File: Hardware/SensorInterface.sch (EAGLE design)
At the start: 57 parts, among them J3 CONN_32.54_SCREW, J4 CONN_32.54_SCREW, J5 CONN_42.54_SCREW, Q1 DMG3404, Q2 2N7002, Q3 2N7002, Q4 DMG3404, Q5 DMG3404, U10 SN74AHC1G86DCK, U11 MCP6041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

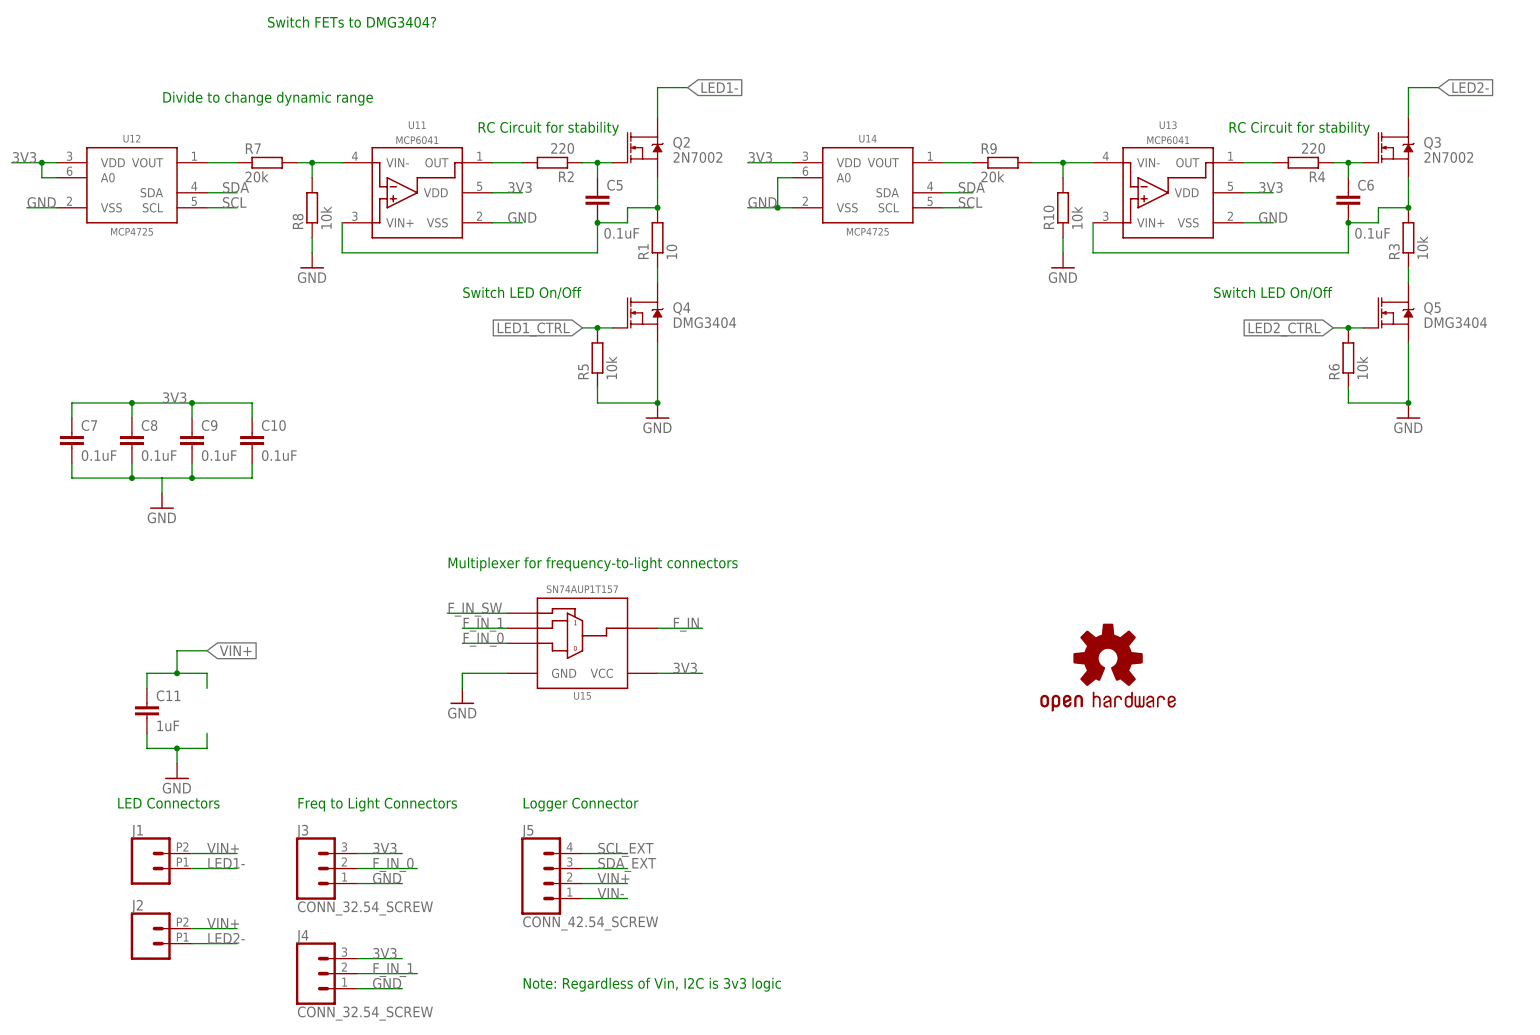
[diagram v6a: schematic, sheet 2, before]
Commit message: Updated breakouts and main board, schematic v0.1 updates
Updated schematic for main unit to v0.1, incorporating updates from testing of v0.0 unit
Minor updates to breakout boards, adding passives and updating components
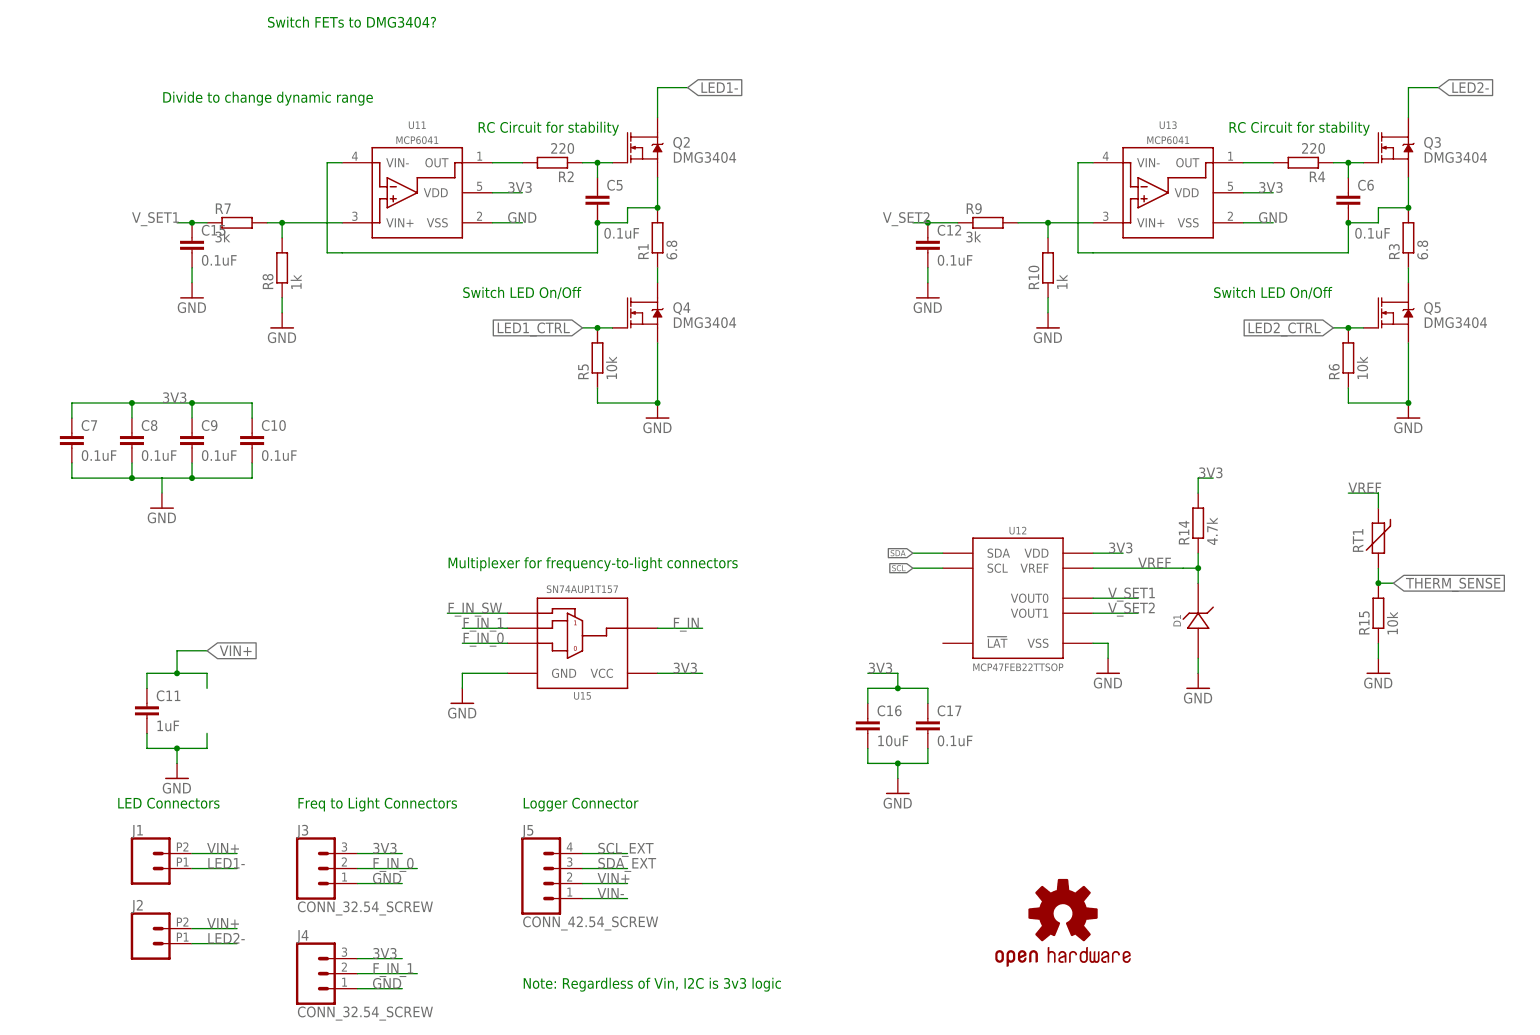
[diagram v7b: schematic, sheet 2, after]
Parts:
- removed U$3: ATTINY441/841841SOIC, bschulz:ATTINY441/841841SOIC
- added C12, C15: 0.1uF, bschulz_passives:C-EU0.1UFC0603
- added C16: 10uF, bschulz_passives:C-EUC0805
- added C17: 0.1uF, bschulz_passives:C-EUC0603
- added D1: (no value), bschulz:LM40402.048
- added R14: 4.7k, bschulz_passives:R-EU_R0603
- added R15: 10k, bschulz_passives:R-EU_P10KR0603
- added RT1: (no value), bschulz:THERMISTOR10K
- added TP1, TP2, TP3, TP4, TP5, TP6, TP7: TESTPOINTRCU, bschulz:TESTPOINTRCU
- added U17: SN74AUP1G08DCK, bschulz:SN74AUP1G08DCK
- Q2, Q3: value 2N7002 -> DMG3404; device bschulz:MOSFET-NCH-2N7002PW -> bschulz:MOSFET-NCH-DMG3404L
- R1: value 10 -> 6.8
- R10, R8: value 10k -> 1k
- R3: value 10k -> 6.8
- R7, R9: value 20k -> 3k
- U12: value MCP4725A1 -> MCP47FEB22TTSOP; device bschulz:MCP4725A1 -> bschulz:MCP47FEB22TTSOP
- U14: value MCP4725A1 -> (none); device bschulz:MCP4725A1 -> bschulz:ATTINY1634QFN
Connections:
- removed net MISO: ISP1.MISO, U$3.PA5
- removed net N$17: R9.1, U14.VOUT
- removed net N$20 (its old number): U4G1.Y, U6.CLK
- removed net N$28: R7.1, U12.VOUT
- new net INT_SET: U17.Y, U8.!PRE
- new net RX: TP2.P$1, U14.PA7
- new net THERM_SENSE: R15.2, RT1.1, U14.PA6
- new net TX: TP1.P$1, U14.PB0
- new net VREF: D1.C, R14.1, RT1.2, U12.VREF
- new net V_SET1: C15.1, R7.1, U12.VOUT0
- new net V_SET2: C12.1, R9.1, U12.VOUT1
- net !CLEAR: now also U14.PA2
- net !F_IN: no longer U8.CLK
- net !INT: now also TP3.P$1, U14.PC2; no longer U$3.PB1
- net !P=Q: now also U17.B; no longer U8.!PRE
- net !RESET: now also U14.PC3; no longer U$3.PB3
- net !SYNCRES: now also U17.A, U6.!CLR
- net 3V3: now also C16.1, C17.1, R14.2, U14.VCC, U17.VCC, U7.!PRE, U8.!CLR; no longer U$3.VCC, U12.A0, U14.VDD
- net ADR_SEL: now also ISP1.MISO, U14.PB2; no longer U$3.PA3
- net CLK: now also U14.PA1
- net DATA: now also U14.PA3
- net F_IN: now also U8.CLK
- net F_IN_SW: now also U14.PA5; no longer U$3.PA2
- net GND: now also C12.2, C15.2, C16.2, C17.2, D1.A, R15.1, TP7.P$1, U14.GND, U17.GND, U6.CLK; no longer U$3.GND, U14.A0, U14.VSS
- net LED1_CTRL: now also U14.PB3; no longer U$3.PA0
- net LED2_CTRL: now also U14.PC0; no longer U$3.PA1
- net N$18: now also U11.VIN+; no longer U11.VIN-
- net N$19: now also U13.VIN-; no longer U13.VIN+
- net N$22: now also U11.VIN-; no longer U11.VIN+
- net N$29: now also U13.VIN+; no longer U13.VIN-
- net SCL: now also TP5.P$1, U14.PC5; no longer U$3.PA7, U14.SCL
- net SCL_EXT: now also U14.PC1; no longer U$3.PA4
- net SDA: now also TP4.P$1, U14.PC4; no longer U$3.PB2, U14.SDA
- net SDA_EXT: now also U14.PB1; no longer U$3.PA6
- net URES: now also TP6.P$1, U14.PA4; no longer U4G1.A
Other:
- note added: "MISO"
- note added: "PWM"
- moved on the sheet: R10, R7, R8, R9, U5G1, U8

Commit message: Reroute initial stage
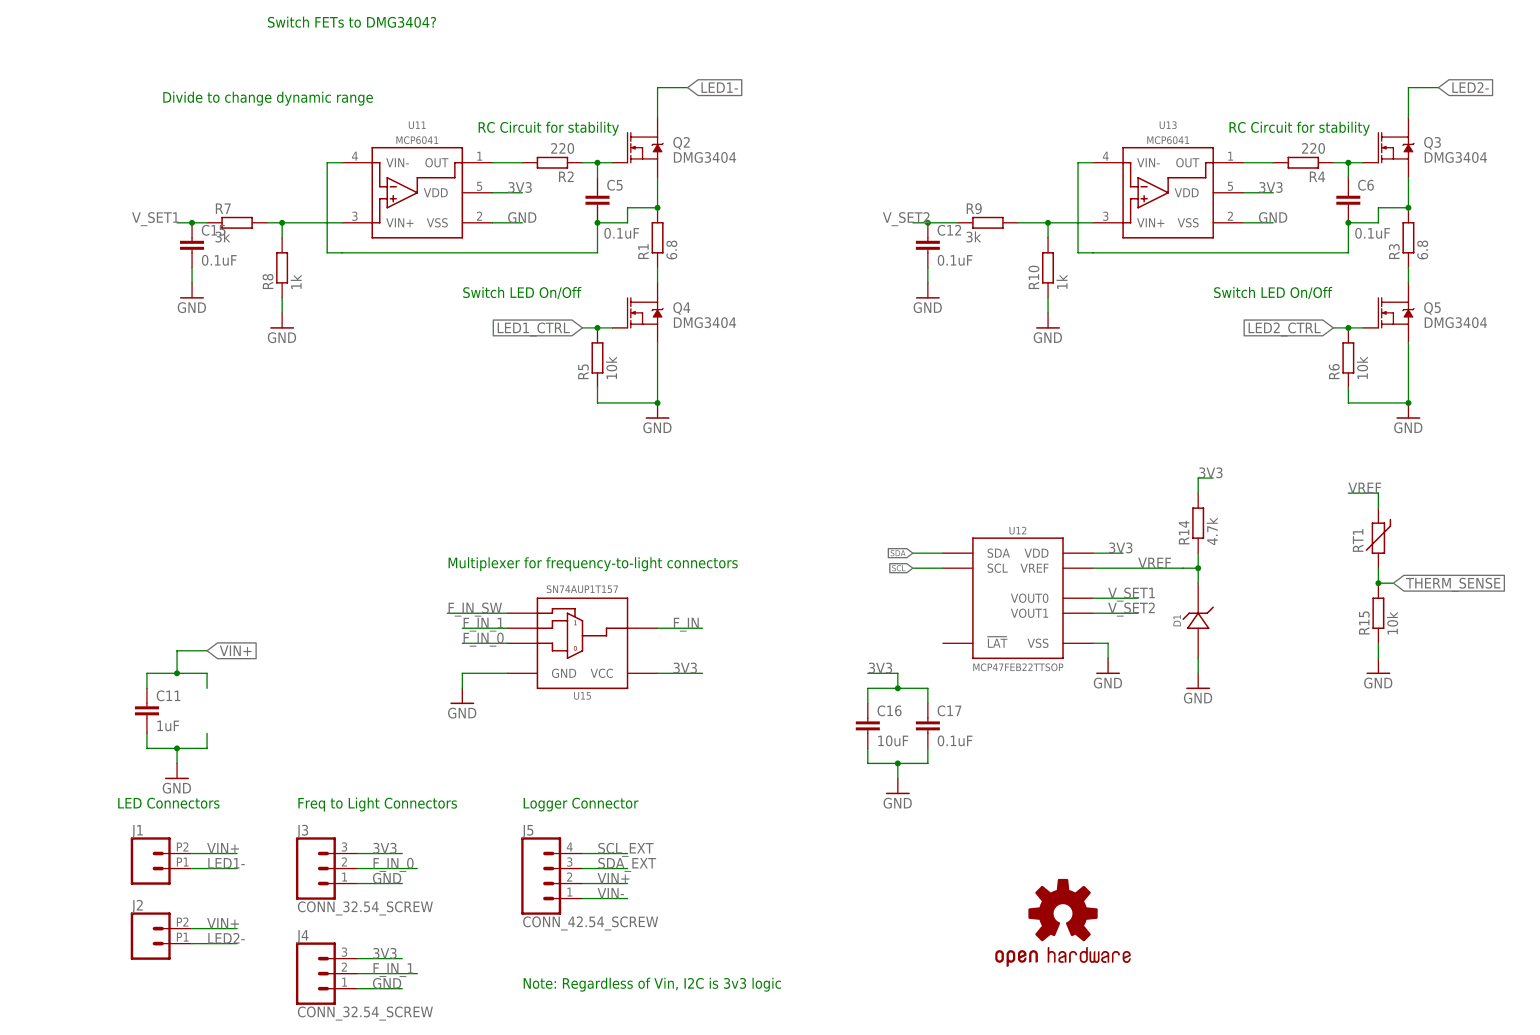
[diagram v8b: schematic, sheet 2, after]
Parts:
- removed C10, C4, C8: 0.1uF, bschulz_passives:C-EUC0603
- C13, C14: device bschulz_passives:C-EUC0603 -> bschulz_passives:C-EU0.1UFC0402
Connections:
- net 3V3: no longer C10.1, C4.1, C8.1
- net GND: no longer C10.2, C4.2, C8.2
